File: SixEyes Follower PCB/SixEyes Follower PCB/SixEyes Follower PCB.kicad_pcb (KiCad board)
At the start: 2 copper layers, 160 x 100 mm, 57 parts, among them J1_MOTOR JST-XH-6-STEPPER, J2_MOTOR JST-XH-6-STEPPER, J3_MOTOR JST-XH-6-STEPPER, J4_MOTOR JST-XH-6-STEPPER, U1A ESP32-S3-SOCK-LEFT, U1B ESP32-S3-SOCK-RIGHT, U2 TMC2209-J1-BASE, U3 TMC2209-J2-SHOULDER-A, U4 TMC2209-J3-SHOULDER-B, U5 TMC2209-J4-ELBOW

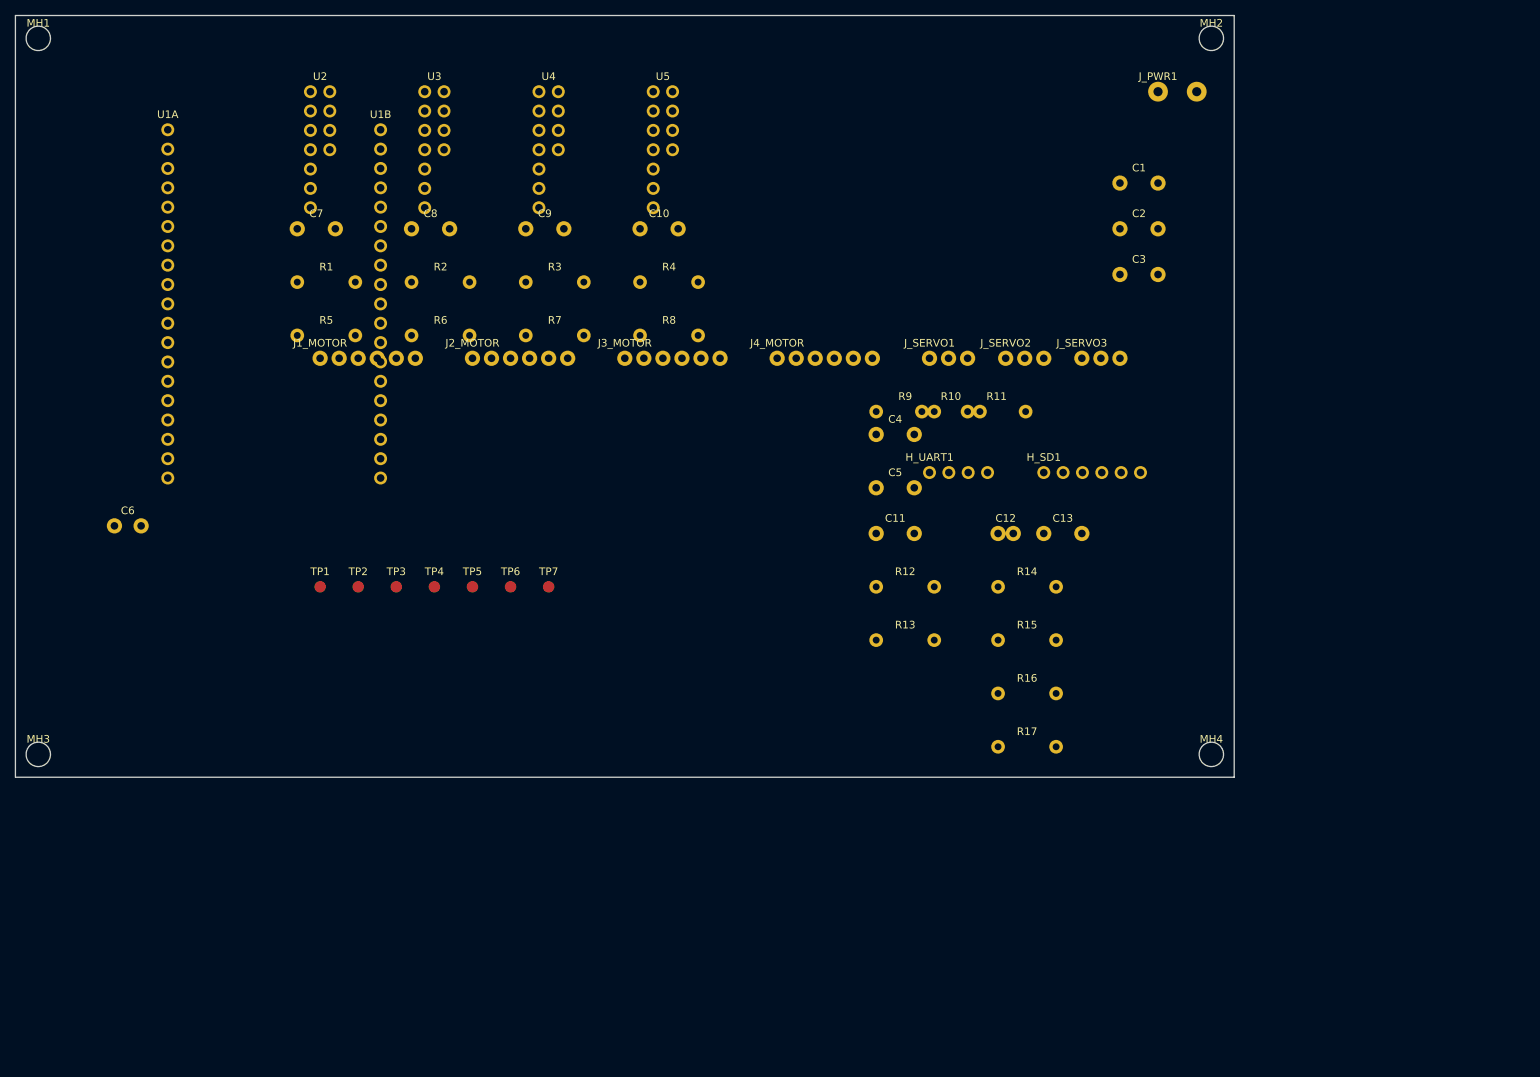
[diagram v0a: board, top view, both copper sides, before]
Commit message: refactor: flatten sixeyes/ to root, add KiCad PCB project, fix JSON pipeline, fix safety bitmask, implement ROS2 nodes, update docs
- Flatten sixeyes/ wrapper: firmware/, ros2_ws/, tools/, simulation/, hardware_assets/ now at repo root
- Merge sixeyes/docs/ into docs/ (safety.md, protocols/uart_protocol.md)
- Add KiCad follower PCB project files (.kicad_pro, .kicad_prl, fp-lib-table, custom footprints, design_inputs/)
- Update .gitignore: exclude KiCad .history/ and *-backups/ directories
- Fix UartJsonParser pipeline: init() now called in MessageRouter::init(), update() ticked each control loop iteration
- Add JOINT_STATE (type 8) to MessageType enum, parse block, struct, and TeleoperationHandler callback
- Fix FaultManager: uint32_t bitmask supports simultaneous faults, add clearFault(f)
- Fix SafetyTask: isSafeToOperate() checks both HeartbeatMonitor and ROS2 alive; use SAFETY_HEARTBEAT_TIMEOUT_MS constant
- Fix main.cpp: UsbCDC::update() now called in loop()
- Fix MotorControlScheduler: 500 Hz (was 400 Hz), UartJsonParser::update() added to control loop
- Implement ROS2 nodes: usb_bridge_node, safety_node, camera_node, joint_state_node
- Update docs: FIRMWARE_FEATURE_INVENTORY, TELEOPERATION_MODE_ARCHITECTURE, JSON_MESSAGE_PROTOCOL, PROJECT_SCOPE_AND_REPO_MAP, README
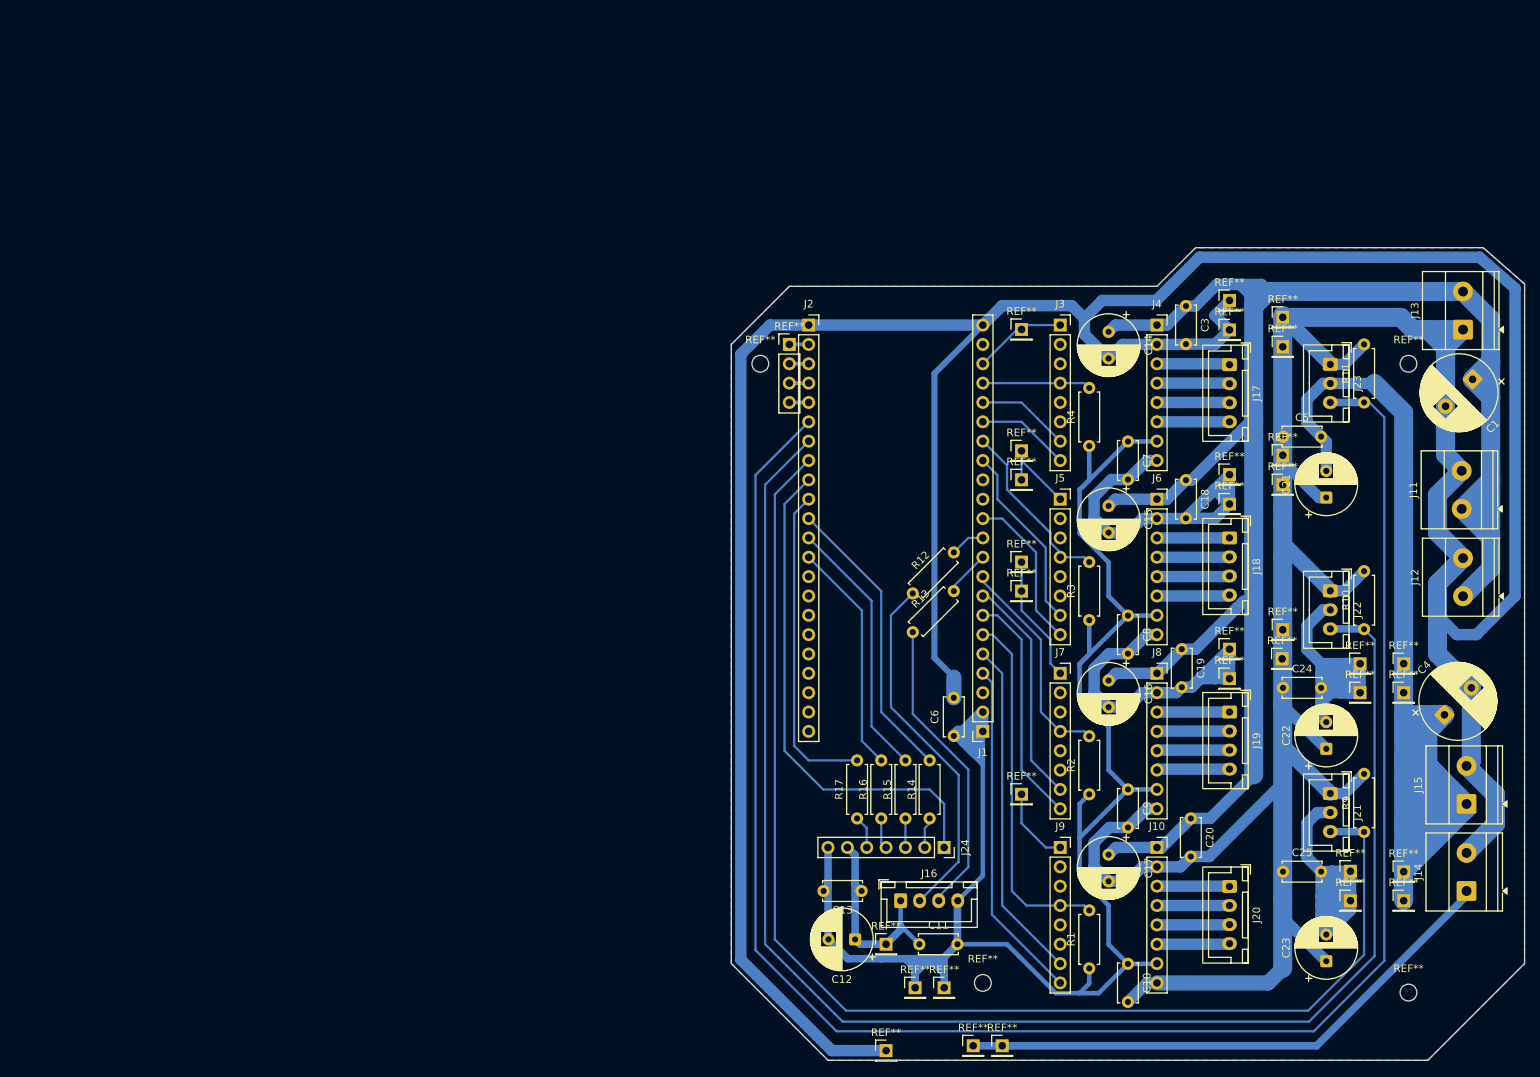
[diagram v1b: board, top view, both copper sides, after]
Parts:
- removed C2: 1uF/50V, Capacitor_THT:C_Disc_D5.0mm_W2.5mm_P5.00mm
- removed H_SD1: HDR-1x06-SD-SPI, Connector_PinHeader_2.54mm:PinHeader_1x06_P2.54mm_Vertical
- removed H_UART1: HDR-1x04-UART, Connector_PinHeader_2.54mm:PinHeader_1x04_P2.54mm_Vertical
- removed J1_MOTOR, J2_MOTOR, J3_MOTOR, J4_MOTOR: JST-XH-6-STEPPER, Connector_JST:JST_XH_B6B-XH-A_1x06_P2.50mm_Vertical
- removed J_PWR1: PWR-IN-24V, TerminalBlock:TerminalBlock_bornier-2_P5.08mm
- removed J_SERVO1, J_SERVO2, J_SERVO3: JST-XH-3-SERVO, Connector_JST:JST_XH_B3B-XH-A_1x03_P2.50mm_Vertical
- removed MH1, MH2, MH3, MH4: MountingHole_M3, MountingHole:MountingHole_3.2mm_M3
- removed R5, R6, R7, R8: 0R DNI, Resistor_THT:R_Axial_DIN0207_L6.3mm_D2.5mm_P7.62mm_Horizontal
- removed TP1: TP_EN_ALL, TestPoint:TestPoint_Pad_D1.5mm
- removed TP2: TP_PDN_J1, TestPoint:TestPoint_Pad_D1.5mm
- removed TP3: TP_PDN_J2, TestPoint:TestPoint_Pad_D1.5mm
- removed TP4: TP_PDN_J3, TestPoint:TestPoint_Pad_D1.5mm
- removed TP5: TP_PDN_J4, TestPoint:TestPoint_Pad_D1.5mm
- removed TP6: TP_UART_RX, TestPoint:TestPoint_Pad_D1.5mm
- removed TP7: TP_UART_TX, TestPoint:TestPoint_Pad_D1.5mm
- removed U1A: ESP32-S3-SOCK-LEFT, Connector_PinSocket_2.54mm:PinSocket_1x19_P2.54mm_Vertical
- removed U1B: ESP32-S3-SOCK-RIGHT, Connector_PinSocket_2.54mm:PinSocket_1x19_P2.54mm_Vertical
- removed U2: TMC2209-J1-BASE, Connector_PinSocket_2.54mm:PinSocket_1x08_P2.54mm_Vertical
- removed U3: TMC2209-J2-SHOULDER-A, Connector_PinSocket_2.54mm:PinSocket_1x08_P2.54mm_Vertical
- removed U4: TMC2209-J3-SHOULDER-B, Connector_PinSocket_2.54mm:PinSocket_1x08_P2.54mm_Vertical
- removed U5: TMC2209-J4-ELBOW, Connector_PinSocket_2.54mm:PinSocket_1x08_P2.54mm_Vertical
- added C14: 10 uF, Capacitor_THT:CP_Radial_D8.0mm_P3.50mm, F.Cu at (143.5, 41.5)
- added C15: 10 uF, Capacitor_THT:CP_Radial_D8.0mm_P3.50mm, F.Cu at (143.5, 64.4)
- added C16: 10 uF, Capacitor_THT:CP_Radial_D8.0mm_P3.50mm, F.Cu at (143.5, 87.3)
- added C17: 10 uF, Capacitor_THT:CP_Radial_D8.0mm_P3.50mm, F.Cu at (143.5, 110.2)
- added C18: 100 nF, Capacitor_THT:C_Disc_D5.0mm_W2.5mm_P5.00mm, F.Cu at (153.7, 61.0)
- added C19: 100 nF, Capacitor_THT:C_Disc_D5.0mm_W2.5mm_P5.00mm, F.Cu at (153.1, 83.2)
- added C20: 100 nF, Capacitor_THT:C_Disc_D5.0mm_W2.5mm_P5.00mm, F.Cu at (154.3, 105.4)
- added C21: 10 uF, Capacitor_THT:CP_Radial_D8.0mm_P3.50mm, F.Cu at (172.1, 63.3)
- added C22: 10 uF, Capacitor_THT:CP_Radial_D8.0mm_P3.50mm, F.Cu at (172.1, 96.3)
- added C23: 10 uF, Capacitor_THT:CP_Radial_D8.0mm_P3.50mm, F.Cu at (172.1, 124.2)
- added C24: 100 nF, Capacitor_THT:C_Disc_D5.0mm_W2.5mm_P5.00mm, F.Cu at (166.4, 88.3)
- added C25: 100 nF, Capacitor_THT:C_Disc_D5.0mm_W2.5mm_P5.00mm, F.Cu at (166.4, 112.4)
- added J1: Conn_01x22_Socket, Connector_PinSocket_2.54mm:PinSocket_1x22_P2.54mm_Vertical, F.Cu at (127.0, 94.0)
- added J10: Conn_01x08_Socket, Connector_PinSocket_2.54mm:PinSocket_1x08_P2.54mm_Vertical, F.Cu at (149.9, 109.2)
- added J11: Conn_01x02, TerminalBlock_Phoenix:TerminalBlock_Phoenix_MKDS-1,5-2_1x02_P5.00mm_Horizontal, F.Cu at (189.9, 64.8)
- added J12: Conn_01x02, TerminalBlock_Phoenix:TerminalBlock_Phoenix_MKDS-1,5-2_1x02_P5.00mm_Horizontal, F.Cu at (190.0, 76.2)
- added J13: Conn_01x02, TerminalBlock_Phoenix:TerminalBlock_Phoenix_MKDS-1,5-2_1x02_P5.00mm_Horizontal, F.Cu at (190.0, 41.2)
- added J14: Conn_01x02, TerminalBlock_Phoenix:TerminalBlock_Phoenix_MKDS-1,5-2_1x02_P5.00mm_Horizontal, F.Cu at (190.5, 114.9)
- added J15: Conn_01x02, TerminalBlock_Phoenix:TerminalBlock_Phoenix_MKDS-1,5-2_1x02_P5.00mm_Horizontal, F.Cu at (190.5, 103.5)
- added J16: JSTXH 4PIN to LEADER, Connector_JST:JST_XH_B4B-XH-A_1x04_P2.50mm_Vertical, F.Cu at (116.2, 116.2)
- added J17: Conn_01x04, Connector_JST:JST_XH_B4B-XH-A_1x04_P2.50mm_Vertical, F.Cu at (159.4, 45.8)
- added J18: Conn_01x04, Connector_JST:JST_XH_B4B-XH-A_1x04_P2.50mm_Vertical, F.Cu at (159.4, 68.6)
- added J19: Conn_01x04, Connector_JST:JST_XH_B4B-XH-A_1x04_P2.50mm_Vertical, F.Cu at (159.4, 91.4)
- added J2: Conn_01x22_Socket, Connector_PinSocket_2.54mm:PinSocket_1x22_P2.54mm_Vertical, F.Cu at (104.1, 40.6)
- added J20: Conn_01x04, Connector_JST:JST_XH_B4B-XH-A_1x04_P2.50mm_Vertical, F.Cu at (159.4, 114.3)
- added J21: Conn_01x03, Connector_JST:JST_XH_B3B-XH-A_1x03_P2.50mm_Vertical, F.Cu at (172.6, 102.1)
- added J22: Conn_01x03, Connector_JST:JST_XH_B3B-XH-A_1x03_P2.50mm_Vertical, F.Cu at (172.6, 75.5)
- added J23: Conn_01x03, Connector_JST:JST_XH_B3B-XH-A_1x03_P2.50mm_Vertical, F.Cu at (172.6, 45.8)
- added J24: DUPONT 7PIN TO SDREADER, Connector_PinSocket_2.54mm:PinSocket_1x07_P2.54mm_Vertical, F.Cu at (121.9, 109.2)
- added J3: Conn_01x08_Socket, Connector_PinSocket_2.54mm:PinSocket_1x08_P2.54mm_Vertical, F.Cu at (137.2, 40.6)
- added J4: Conn_01x08_Socket, Connector_PinSocket_2.54mm:PinSocket_1x08_P2.54mm_Vertical, F.Cu at (149.9, 40.6)
- added J5: Conn_01x08_Socket, Connector_PinSocket_2.54mm:PinSocket_1x08_P2.54mm_Vertical, F.Cu at (137.2, 63.5)
- added J6: Conn_01x08_Socket, Connector_PinSocket_2.54mm:PinSocket_1x08_P2.54mm_Vertical, F.Cu at (149.9, 63.5)
- added J7: Conn_01x08_Socket, Connector_PinSocket_2.54mm:PinSocket_1x08_P2.54mm_Vertical, F.Cu at (137.2, 86.4)
- added J8: Conn_01x08_Socket, Connector_PinSocket_2.54mm:PinSocket_1x08_P2.54mm_Vertical, F.Cu at (149.9, 86.4)
- added J9: Conn_01x08_Socket, Connector_PinSocket_2.54mm:PinSocket_1x08_P2.54mm_Vertical, F.Cu at (137.2, 109.2)
- added REF**: PinHeader_1x01_P2.54mm_Vertical, Connector_PinHeader_2.54mm:PinHeader_1x01_P2.54mm_Vertical, F.Cu at (166.4, 80.6)
- added REF**: PinHeader_1x01_P2.54mm_Vertical, Connector_PinHeader_2.54mm:PinHeader_1x01_P2.54mm_Vertical, F.Cu at (114.3, 121.9)
- added REF**: PinHeader_1x01_P2.54mm_Vertical, Connector_PinHeader_2.54mm:PinHeader_1x01_P2.54mm_Vertical, F.Cu at (159.4, 37.4)
- added REF**: PinHeader_1x01_P2.54mm_Vertical, Connector_PinHeader_2.54mm:PinHeader_1x01_P2.54mm_Vertical, F.Cu at (132.1, 102.2)
- added REF**: PinHeader_1x01_P2.54mm_Vertical, Connector_PinHeader_2.54mm:PinHeader_1x01_P2.54mm_Vertical, F.Cu at (159.4, 64.1)
- added REF**: PinHeader_1x01_P2.54mm_Vertical, Connector_PinHeader_2.54mm:PinHeader_1x01_P2.54mm_Vertical, F.Cu at (114.3, 135.9)
- added REF**: PinHeader_1x01_P2.54mm_Vertical, Connector_PinHeader_2.54mm:PinHeader_1x01_P2.54mm_Vertical, F.Cu at (132.1, 61.0)
- added REF**: MountingHole_2.2mm_M2, MountingHole:MountingHole_2.2mm_M2, F.Cu at (182.9, 45.7)
- added REF**: MountingHole_2.2mm_M2, MountingHole:MountingHole_2.2mm_M2, F.Cu at (127.0, 127.0)
- added REF**: PinHeader_1x01_P2.54mm_Vertical, Connector_PinHeader_2.54mm:PinHeader_1x01_P2.54mm_Vertical, F.Cu at (182.2, 112.4)
- added REF**: MountingHole_2.2mm_M2, MountingHole:MountingHole_2.2mm_M2, F.Cu at (182.9, 128.3)
- added REF**: PinHeader_1x01_P2.54mm_Vertical, Connector_PinHeader_2.54mm:PinHeader_1x01_P2.54mm_Vertical, F.Cu at (176.5, 88.9)
- added REF**: PinHeader_1x01_P2.54mm_Vertical, Connector_PinHeader_2.54mm:PinHeader_1x01_P2.54mm_Vertical, F.Cu at (175.3, 112.3)
- added REF**: PinHeader_1x01_P2.54mm_Vertical, Connector_PinHeader_2.54mm:PinHeader_1x01_P2.54mm_Vertical, F.Cu at (166.4, 61.6)
- added REF**: PinHeader_1x01_P2.54mm_Vertical, Connector_PinHeader_2.54mm:PinHeader_1x01_P2.54mm_Vertical, F.Cu at (175.3, 116.2)
- added REF**: PinHeader_1x01_P2.54mm_Vertical, Connector_PinHeader_2.54mm:PinHeader_1x01_P2.54mm_Vertical, F.Cu at (182.2, 116.2)
- added REF**: PinHeader_1x01_P2.54mm_Vertical, Connector_PinHeader_2.54mm:PinHeader_1x01_P2.54mm_Vertical, F.Cu at (129.5, 135.3)
- added REF**: MountingHole_2.2mm_M2, MountingHole:MountingHole_2.2mm_M2, F.Cu at (97.8, 45.7)
- added REF**: PinHeader_1x01_P2.54mm_Vertical, Connector_PinHeader_2.54mm:PinHeader_1x01_P2.54mm_Vertical, F.Cu at (182.2, 88.9)
- added REF**: PinHeader_1x01_P2.54mm_Vertical, Connector_PinHeader_2.54mm:PinHeader_1x01_P2.54mm_Vertical, F.Cu at (182.2, 85.1)
- added REF**: PinHeader_1x01_P2.54mm_Vertical, Connector_PinHeader_2.54mm:PinHeader_1x01_P2.54mm_Vertical, F.Cu at (166.4, 57.7)
- added REF**: PinHeader_1x01_P2.54mm_Vertical, Connector_PinHeader_2.54mm:PinHeader_1x01_P2.54mm_Vertical, F.Cu at (166.3, 84.5)
- added REF**: PinHeader_1x01_P2.54mm_Vertical, Connector_PinHeader_2.54mm:PinHeader_1x01_P2.54mm_Vertical, F.Cu at (159.4, 41.3)
- added REF**: PinHeader_1x01_P2.54mm_Vertical, Connector_PinHeader_2.54mm:PinHeader_1x01_P2.54mm_Vertical, F.Cu at (132.1, 41.2)
- added REF**: PinHeader_1x01_P2.54mm_Vertical, Connector_PinHeader_2.54mm:PinHeader_1x01_P2.54mm_Vertical, F.Cu at (132.1, 57.1)
- added REF**: PinHeader_1x01_P2.54mm_Vertical, Connector_PinHeader_2.54mm:PinHeader_1x01_P2.54mm_Vertical, F.Cu at (159.4, 83.2)
- added REF**: PinHeader_1x01_P2.54mm_Vertical, Connector_PinHeader_2.54mm:PinHeader_1x01_P2.54mm_Vertical, F.Cu at (166.4, 43.5)
- added REF**: PinHeader_1x01_P2.54mm_Vertical, Connector_PinHeader_2.54mm:PinHeader_1x01_P2.54mm_Vertical, F.Cu at (176.5, 85.1)
- added REF**: PinHeader_1x01_P2.54mm_Vertical, Connector_PinHeader_2.54mm:PinHeader_1x01_P2.54mm_Vertical, F.Cu at (159.4, 60.3)
- added REF**: PinHeader_1x04_P2.54mm_Vertical, Connector_PinHeader_2.54mm:PinHeader_1x04_P2.54mm_Vertical, F.Cu at (101.6, 43.2)
- added REF**: PinHeader_1x01_P2.54mm_Vertical, Connector_PinHeader_2.54mm:PinHeader_1x01_P2.54mm_Vertical, F.Cu at (125.7, 135.3)
- added REF**: PinHeader_1x01_P2.54mm_Vertical, Connector_PinHeader_2.54mm:PinHeader_1x01_P2.54mm_Vertical, F.Cu at (118.1, 127.6)
- added REF**: PinHeader_1x01_P2.54mm_Vertical, Connector_PinHeader_2.54mm:PinHeader_1x01_P2.54mm_Vertical, F.Cu at (159.4, 87.1)
- added REF**: PinHeader_1x01_P2.54mm_Vertical, Connector_PinHeader_2.54mm:PinHeader_1x01_P2.54mm_Vertical, F.Cu at (132.1, 75.6)
- added REF**: PinHeader_1x01_P2.54mm_Vertical, Connector_PinHeader_2.54mm:PinHeader_1x01_P2.54mm_Vertical, F.Cu at (166.4, 39.6)
- added REF**: PinHeader_1x01_P2.54mm_Vertical, Connector_PinHeader_2.54mm:PinHeader_1x01_P2.54mm_Vertical, F.Cu at (121.9, 127.6)
- added REF**: PinHeader_1x01_P2.54mm_Vertical, Connector_PinHeader_2.54mm:PinHeader_1x01_P2.54mm_Vertical, F.Cu at (132.1, 71.8)
- C1: value 470uF/35V -> 470 uF
- C10, C11, C13, C3, C5, C7, C8, C9: value 100nF -> 100 nF
- C12: value 10uF/10V -> 10 uF; footprint Capacitor_THT:CP_Radial_D5.0mm_P2.00mm -> Capacitor_THT:CP_Radial_D8.0mm_P3.50mm
- C4: value 1000uF/16V -> 1000 uF
- C6: value 220uF/10V -> 220 uF; footprint Capacitor_THT:CP_Radial_D8.0mm_P3.50mm -> Capacitor_THT:C_Disc_D5.0mm_W2.5mm_P5.00mm
- R1, R2, R3, R4: value 4.7k -> 4.7 k
- R12, R13: value 220R DNI -> 220
- R14, R15, R16, R17: value 33R DNI -> 220
- moved R1 137.6 mm to (141.0, 125.1), turned to 90 degrees
- moved C10 115.8 mm to (146.1, 124.5), turned to -90 degrees
- moved C6 113.6 mm to (123.2, 94.6), turned to 90 degrees
- moved C7 112.6 mm to (146.1, 55.9), turned to -90 degrees
- moved R2 111.5 mm to (141.0, 102.2), turned to 90 degrees
- moved C9 108.0 mm to (146.1, 101.6), turned to -90 degrees
- moved C8 106.9 mm to (146.1, 78.8), turned to -90 degrees
- moved R3 86.3 mm to (141.0, 79.4), turned to 90 degrees
- moved R9 84.5 mm to (177.1, 107.2), turned to 90 degrees
- moved C4 83.2 mm to (187.6, 91.8), turned to 45 degrees
- moved R10 64.7 mm to (177.1, 80.6), turned to 90 degrees
- moved R4 62.8 mm to (141.0, 56.5), turned to 90 degrees
- moved C12 56.5 mm to (110.2, 121.3), turned to 180 degrees
- moved C11 54.2 mm to (118.7, 121.9)
- moved C5 53.8 mm to (166.4, 55.3)
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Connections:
- net +24V_MOTOR renamed /+24V_MOTOR
- net SD_CS renamed /SD_CS
- net SD_MISO renamed /SD_SCK
- net SD_MOSI renamed /SD_MOSI
- net SD_SCK renamed /SD_MISO
- net UART_LEADER_RX renamed /UART_LEADER_RX
- net UART_LEADER_TX renamed /UART_LEADER_TX
- C1 pad 2: GND -> /GND
- C10 pad 1: +3V3_LOGIC -> /+3V3_LOGIC
- C10 pad 2: GND -> /GND
- C11 pad 1: +3V3_LOGIC -> /GND
- C11 pad 2: GND -> /+3V3_LOGIC
- C12 pad 1: +3V3_LOGIC -> /GND
- C12 pad 2: GND -> /+3V3_LOGIC
- C13 pad 1: +3V3_LOGIC -> /GND
- C13 pad 2: GND -> /+3V3_LOGIC
- C3 pad 2: GND -> /GND
- C4 pad 1: +6V6_SERVO -> /+6V6_SERVO
- C4 pad 2: GND -> /GND
- C5 pad 1: +6V6_SERVO -> /GND
- C5 pad 2: GND -> /+6V6_SERVO
- C6 pad 1: +3V3_LOGIC -> /+3V3_LOGIC
- C6 pad 2: GND -> /GND
- C7 pad 1: +3V3_LOGIC -> /+3V3_LOGIC
- C7 pad 2: GND -> /GND
- C8 pad 1: +3V3_LOGIC -> /+3V3_LOGIC
- C8 pad 2: GND -> /GND
- C9 pad 1: +3V3_LOGIC -> /+3V3_LOGIC
- C9 pad 2: GND -> /GND
- R1 pad 1: +3V3_LOGIC -> /+3V3_LOGIC
- R1 pad 2: PDN_J1 -> /PDN_J4
- R10 pad 1: SERVO_WRIST_YAW -> /SERVO_WRIST_YAW
- R10 pad 2: GND -> /GND
- R11 pad 1: SERVO_GRIPPER -> /SERVO_GRIPPER
- R11 pad 2: GND -> /GND
- R2 pad 1: +3V3_LOGIC -> /+3V3_LOGIC
- R2 pad 2: PDN_J2 -> /PDN_J3
- R3 pad 1: +3V3_LOGIC -> /+3V3_LOGIC
- R3 pad 2: PDN_J3 -> /PDN_J2
- R4 pad 1: +3V3_LOGIC -> /+3V3_LOGIC
- R4 pad 2: PDN_J4 -> /PDN_J1
- R9 pad 1: SERVO_WRIST_PITCH -> /SERVO_WRIST_PITCH
- R9 pad 2: GND -> /GND
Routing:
- net /GND: track 0.00 -> 803.4 mm
- net /+3V3_LOGIC: track 0.00 -> 342.0 mm
- net /+6V6_SERVO: track 0.00 -> 322.6 mm
- net /+24V_MOTOR: track 0.00 -> 255.6 mm
- net /SERVO_GRIPPER: track 0.00 -> 242.3 mm
- net /SERVO_WRIST_YAW: track 0.00 -> 204.1 mm
- net /SERVO_WRIST_PITCH: track 0.00 -> 169.5 mm
- net /SD_CD: track 0.00 -> 66.4 mm
- net /UART_LEADER_RX: track 0.00 -> 51.9 mm
- net /EN_ALL: track 0.00 -> 51.4 mm
- net /PDN_J4: track 0.00 -> 47.2 mm
- net /SD_CS: track 0.00 -> 46.6 mm
- net /UART_LEADER_TX: track 0.00 -> 45.9 mm
- net /STEP_J4: track 0.00 -> 44.8 mm
- net /DIR_J4: track 0.00 -> 44.8 mm
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- added copper zone on B.Cu, net /GND
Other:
- board size 160 x 100 mm -> 104.1 x 106.7 mm
